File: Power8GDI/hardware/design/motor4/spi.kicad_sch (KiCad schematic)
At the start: 8 parts, among them U6190 SN74LVC1G125QDBVRQ1

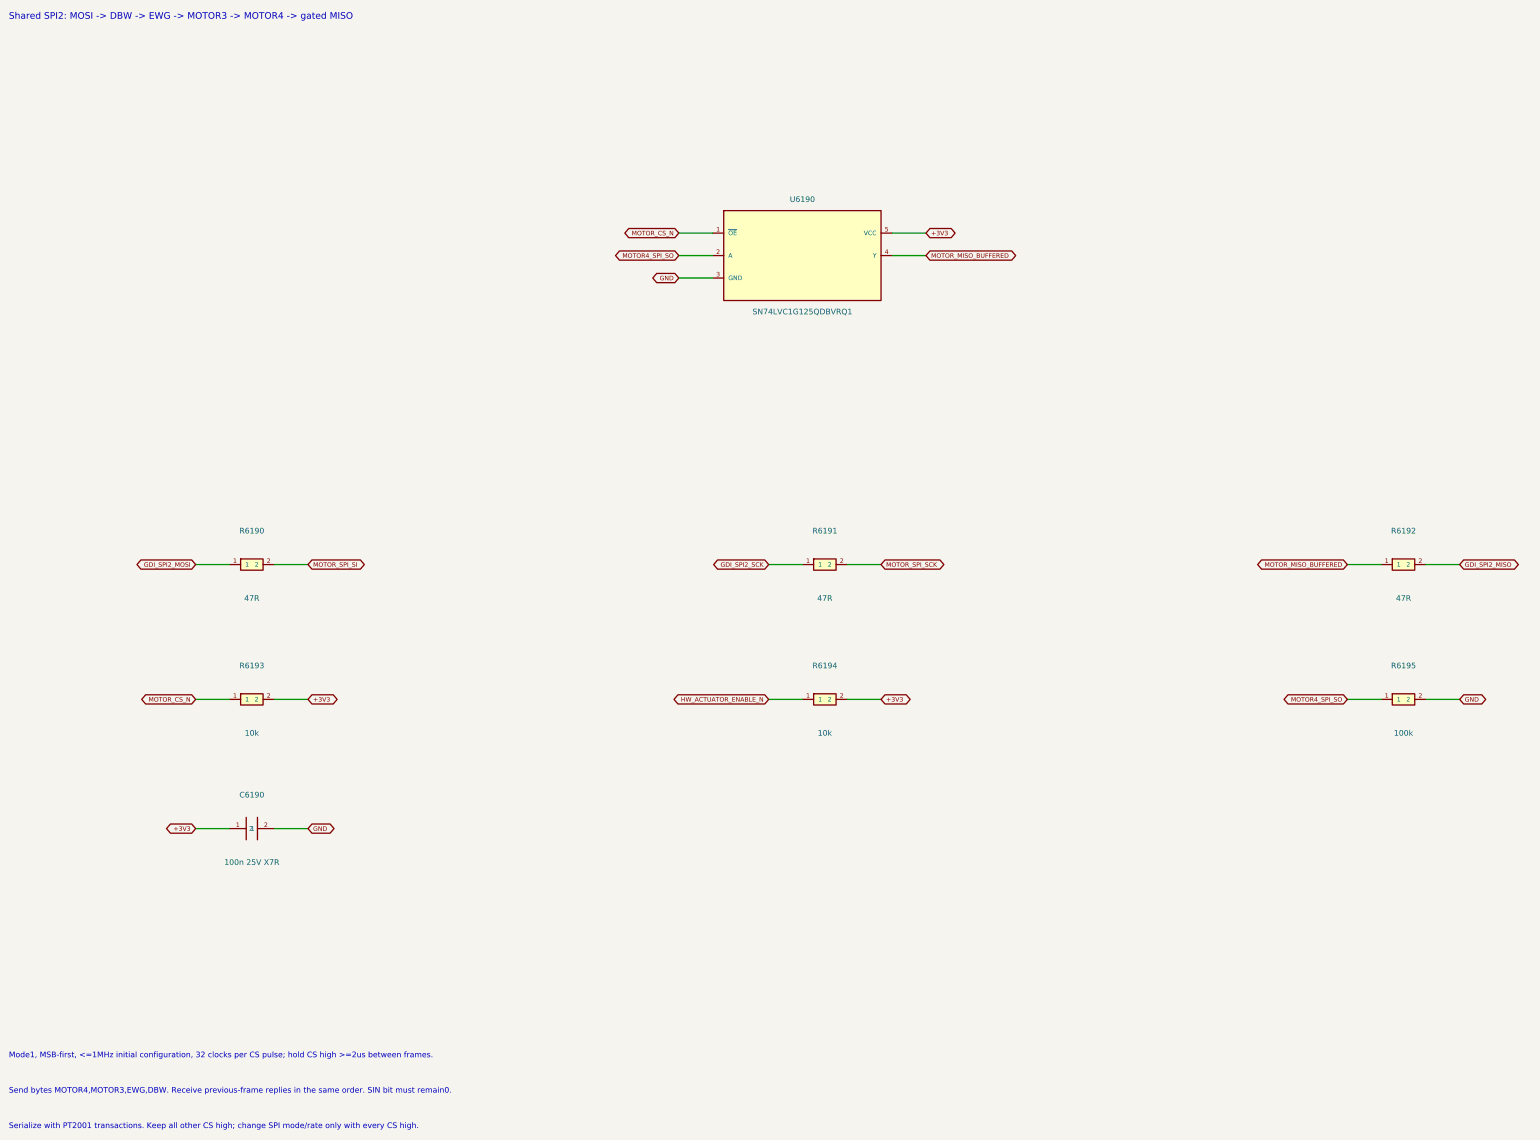
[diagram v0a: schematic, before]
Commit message: Redesign sport target as six DI/PI channels with two motors and one lambda
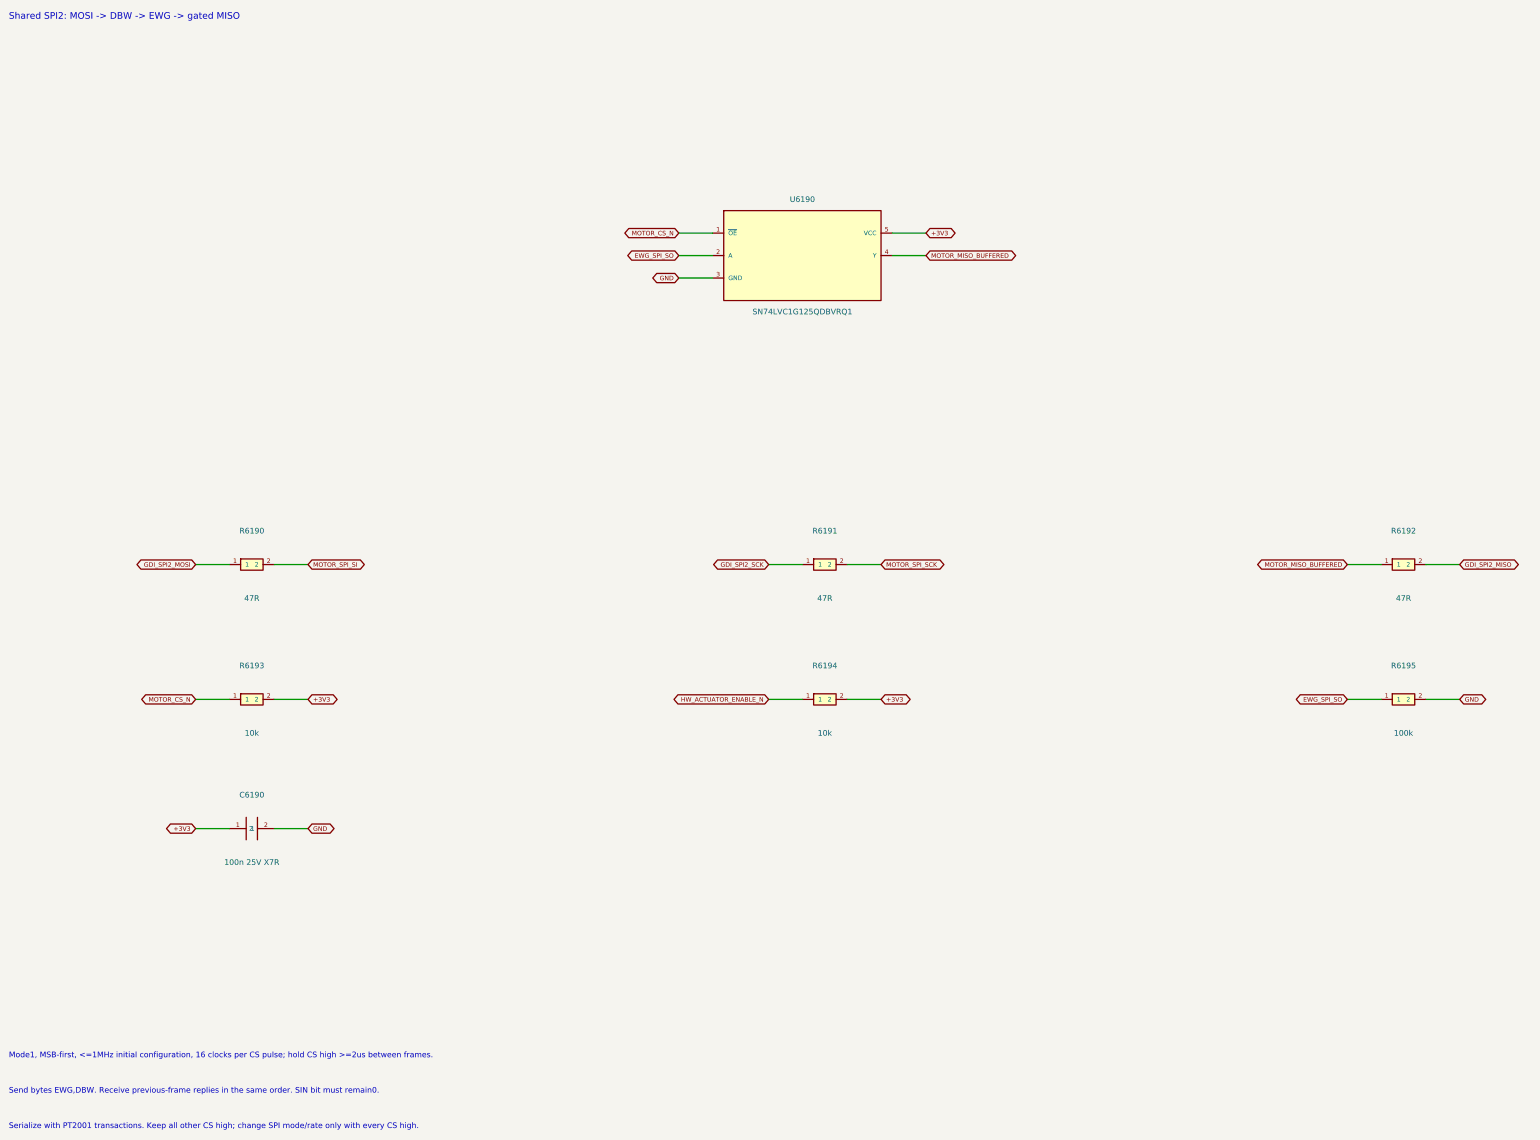
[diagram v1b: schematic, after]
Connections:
- net MOTOR4_SPI_SO renamed EWG_SPI_SO
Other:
- note added: "Mode1, MSB-first, <=1MHz initial configuration, 16 clocks per CS pulse; hold CS high >=2us between frames."
- note added: "Send bytes EWG,DBW. Receive previous-frame replies in the same order. SIN bit must remain0."
- note added: "Shared SPI2: MOSI -> DBW -> EWG -> gated MISO"
- note removed: "Mode1, MSB-first, <=1MHz initial configuration, 32 clocks per CS pulse; hold CS high >=2us between frames."
- note removed: "Send bytes MOTOR4,MOTOR3,EWG,DBW. Receive previous-frame replies in the same order. SIN bit must remain0."
- note removed: "Shared SPI2: MOSI -> DBW -> EWG -> MOTOR3 -> MOTOR4 -> gated MISO"
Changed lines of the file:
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@@
 (kicad_sch (version 20250114) (generator "eeschema") (paper "A3") (title_block (title "Motor daisy chain and shared SPI isolation") (rev "Engineering draft 0.1") (comment 1 "UNQUALIFIED: no manufacturing or engine approval"))
-(text "Shared SPI2: MOSI -> DBW -> EWG -> MOTOR3 -> MOTOR4 -> gated MISO" (at 20 15 0) (effects (font (size 1.5 1.5)) (justify left top)))
+(text "Shared SPI2: MOSI -> DBW -> EWG -> gated MISO" (at 20 15 0) (effects (font (size 1.5 1.5)) (justify left top)))
 (symbol (lib_id "Power8GDI_Motor4:SN74LVC1G125_Q1") (at 199.39 69.85 0) (unit 1) (in_bom yes) (on_board yes) (dnp no) (property "Reference" "U6190" (at 199.39 57.14999999999999 0) (effects (font (size 1.27 1.27)))) (property "Value" "SN74LVC1G125QDBVRQ1" (at 199.39 82.55 0) (effects (font (size 1.27 1.27)))) (property "Footprint" "Package_TO_SOT_SMD:SOT-23-5" (at 199.39 69.85 0) (effects (font (size 1.27 1.27)) (hide yes))) (property "Design note" "Extra explicit MISO isolation. TLE SO is tri-state at CSN high; asynchronous fault flag exists while CSN low before first clock, per Infineon4.12.1." (at 199.39 69.85 0) (effects (font (size 1.27 1.27)) (hide yes))) (pin "1") (pin "2") (pin "3") (pin "5") (pin "4") (instances (project "Power8GDI_Core" (path "/f4d21065-0a5b-5086-a08e-1af9469f04bd/653a7828-1657-5b98-8bae-fc4d9e0f409d" (reference "U6190") (unit 1))) (project "spi" (path "/73a8af16-0669-5b86-9557-39b951c36023" (reference "U6190") (unit 1)))))
 (wire (pts (xy 179.07 64.77) (xy 171.45 64.77)) (stroke (width 0) (type default)))
 (global_label "MOTOR_CS_N" (shape bidirectional) (at 171.45 64.77 0) (effects (font (size 1.016 1.016)) (justify right bottom)))
 (wire (pts (xy 179.07 69.85) (xy 171.45 69.85)) (stroke (width 0) (type default)))
-(global_label "MOTOR4_SPI_SO" (shape bidirectional) (at 171.45 69.85 0) (effects (font (size 1.016 1.016)) (justify right bottom)))
+(global_label "EWG_SPI_SO" (shape bidirectional) (at 171.45 69.85 0) (effects (font (size 1.016 1.016)) (justify right bottom)))
 (wire (pts (xy 179.07 74.93) (xy 171.45 74.93)) (stroke (width 0) (type default)))
 (global_label "GND" (shape bidirectional) (at 171.45 74.93 0) (effects (font (size 1.016 1.016)) (justify right bottom)))
@@
 (symbol (lib_id "Power8GDI_Motor4:Motor_R") (at 335.28 170.18 0) (unit 1) (in_bom yes) (on_board yes) (dnp no) (property "Reference" "R6195" (at 335.28 162.56 0) (effects (font (size 1.27 1.27)))) (property "Value" "100k" (at 335.28 177.8 0) (effects (font (size 1.27 1.27)))) (property "Footprint" "Resistor_SMD:R_0603_1608Metric" (at 335.28 170.18 0) (effects (font (size 1.27 1.27)) (hide yes))) (property "Design note" "" (at 335.28 170.18 0) (effects (font (size 1.27 1.27)) (hide yes))) (pin "1") (pin "2") (instances (project "Power8GDI_Core" (path "/f4d21065-0a5b-5086-a08e-1af9469f04bd/653a7828-1657-5b98-8bae-fc4d9e0f409d" (reference "R6195") (unit 1))) (project "spi" (path "/73a8af16-0669-5b86-9557-39b951c36023" (reference "R6195") (unit 1)))))
 (wire (pts (xy 330.2 170.18) (xy 322.58 170.18)) (stroke (width 0) (type default)))
-(global_label "MOTOR4_SPI_SO" (shape bidirectional) (at 322.58 170.18 0) (effects (font (size 1.016 1.016)) (justify right bottom)))
+(global_label "EWG_SPI_SO" (shape bidirectional) (at 322.58 170.18 0) (effects (font (size 1.016 1.016)) (justify right bottom)))
 (wire (pts (xy 340.36 170.18) (xy 347.98 170.18)) (stroke (width 0) (type default)))
 (global_label "GND" (shape bidirectional) (at 347.98 170.18 180) (effects (font (size 1.016 1.016)) (justify left bottom)))
@@
 (wire (pts (xy 80.01 199.39) (xy 87.63 199.39)) (stroke (width 0) (type default)))
 (global_label "GND" (shape bidirectional) (at 87.63 199.39 180) (effects (font (size 1.016 1.016)) (justify left bottom)))
-(text "Mode1, MSB-first, <=1MHz initial configuration, 32 clocks per CS pulse; hold CS high >=2us between frames." (at 20 250 0) (effects (font (size 1.27 1.27)) (justify left top)))
-(text "Send bytes MOTOR4,MOTOR3,EWG,DBW. Receive previous-frame replies in the same order. SIN bit must remain0." (at 20 258 0) (effects (font (size 1.27 1.27)) (justify left top)))
+(text "Mode1, MSB-first, <=1MHz initial configuration, 16 clocks per CS pulse; hold CS high >=2us between frames." (at 20 250 0) (effects (font (size 1.27 1.27)) (justify left top)))
+(text "Send bytes EWG,DBW. Receive previous-frame replies in the same order. SIN bit must remain0." (at 20 258 0) (effects (font (size 1.27 1.27)) (justify left top)))
 (text "Serialize with PT2001 transactions. Keep all other CS high; change SPI mode/rate only with every CS high." (at 20 266 0) (effects (font (size 1.27 1.27)) (justify left top)))
 (sheet_instances (path "/" (page "1"))))

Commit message: Review B58 injector power stage and bind selected GDI6 BOM
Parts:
- C6190: Hardware_Qualification (none) -> BOARD_QUALIFICATION_PENDING; MPN (none) -> C0805C104K1RACTU; Manufacturer (none) -> KEMET; Procurement_Status (none) -> SELECTED_CATALOG_ITEM; Purchase_Released (none) -> false; Selection_Gaps (none) -> []; Selection_ID (none) -> SEL-50b208aec5b1; Selection_Ratings (none) -> {"capacitance_pf": 100000, "dielectric": "X7R", "rated_volt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; Selection_Source_URLs (none) -> https://www.mouser.com/datasheet/3/72/1/C0805C104K1RACTU.pdf
- R6190, R6191, R6192: Hardware_Qualification (none) -> BOARD_QUALIFICATION_PENDING; MPN (none) -> CRCW060347R0FKEA; Manufacturer (none) -> Vishay; Procurement_Status (none) -> SELECTED_FAMILY_CODE; Purchase_Released (none) -> false; Selection_Gaps (none) -> []; Selection_ID (none) -> SEL-092784c899c7; Selection_Ratings (none) -> {"aec_q200": true, "derating": "Use manufacturer power vers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; Selection_Source_URLs (none) -> https://www.vishay.com/docs/20035/dcrcwe3.pdf
- R6193, R6194: Hardware_Qualification (none) -> BOARD_QUALIFICATION_PENDING; MPN (none) -> CRCW060310K0FKEA; Manufacturer (none) -> Vishay; Procurement_Status (none) -> SELECTED_FAMILY_CODE; Purchase_Released (none) -> false; Selection_Gaps (none) -> []; Selection_ID (none) -> SEL-9c0806476875; Selection_Ratings (none) -> {"aec_q200": true, "derating": "Use manufacturer power vers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; Selection_Source_URLs (none) -> https://www.vishay.com/docs/20035/dcrcwe3.pdf
- R6195: Hardware_Qualification (none) -> BOARD_QUALIFICATION_PENDING; MPN (none) -> CRCW0603100KFKEA; Manufacturer (none) -> Vishay; Procurement_Status (none) -> SELECTED_FAMILY_CODE; Purchase_Released (none) -> false; Selection_Gaps (none) -> []; Selection_ID (none) -> SEL-4e3f06cba0aa; Selection_Ratings (none) -> {"aec_q200": true, "derating": "Use manufacturer power vers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; Selection_Source_URLs (none) -> https://www.vishay.com/docs/20035/dcrcwe3.pdf
- U6190: Hardware_Qualification (none) -> PINOUT_RATINGS_AND_DELIVERY_SUFFIX_REVIEW_PENDING; MPN (none) -> SN74LVC1G125QDBVRQ1; Manufacturer (none) -> Texas Instruments; Procurement_Status (none) -> REFERENCE_MPN_RETAINED; Purchase_Released (none) -> false; Selection_Gaps (none) -> ["Existing schematic MPN retained. Complete circuit rating/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; Selection_ID (none) -> SEL-7081e006b06b; Selection_Ratings (none) -> {}; Selection_Source_URLs (none) -> https://www.ti.com/product/SN74LVC1G125-Q1/part-details/SN7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
